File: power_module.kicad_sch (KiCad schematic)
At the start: 46 parts, among them J1 USB_C_PD, Q1 DUAL_N_FET, Q2 DUAL_N_FET, SW1 OFF, U1 BQ7692003, U2 CH224K, U3 BQ24650

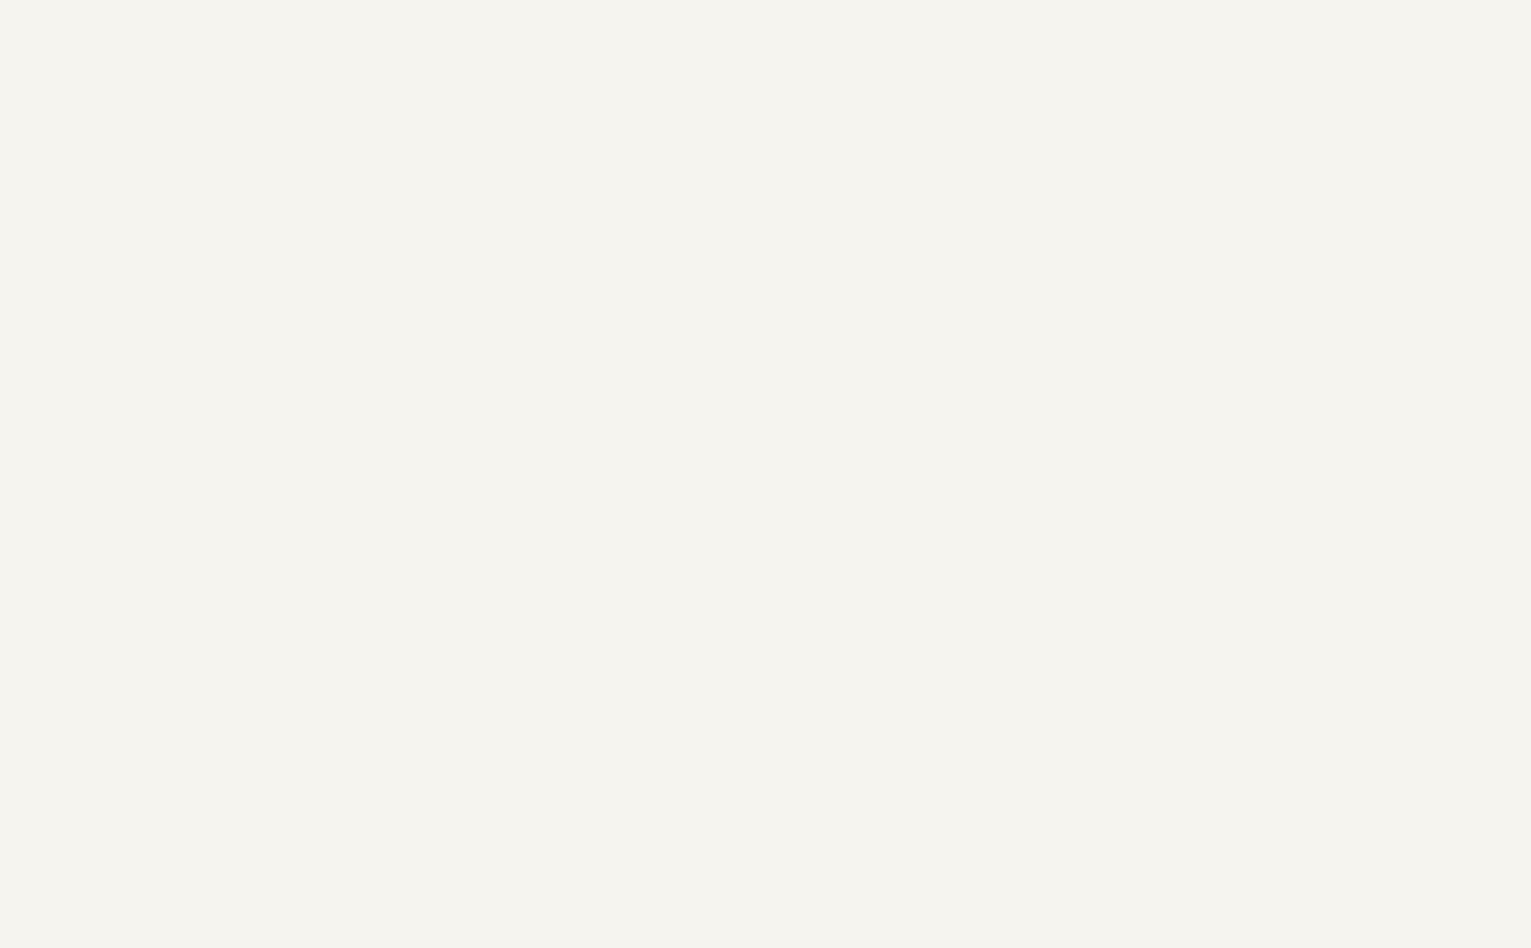
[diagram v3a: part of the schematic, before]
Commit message: schematic: add 4-switch buck-boost output stage (LM5176)
LM5176PWP HTSSOP-28 controller drives 2x dual N-FET pairs (Q3 input,
Q4 output) through inductor L2 (10 µH).  Topology:
  BAT+ → Q3a (HS_IN) → SW1 → L2 → SW2 → Q4b (HS_OUT) → V12_OUT
                ↓                          ↓
         Q3b (LS_IN)→GND          Q4a (LS_OUT)→GND
  + ISNS shunt R20 (5 mΩ) between Q4b drain and V12_OUT load.

Regulation: VFB divider R21=90k / R22=10k → 12 V at FB=1.207 V.
Soft-start C22=10 nF, RT/SYNC R25=22k (~440 kHz), Type II compensation
C20/R26/C21 on COMP, slope cap C31=47 pF.  Mode pin tied to GND for
auto-PFM at light load.

Power: input bulk + HF caps on BAT+ side (C27/C28), output bulk + HF
on V12_OUT (C29/C30), bootstrap caps C23/C24 between BOOT and SW.
VCC self-biased: BIAS tied to VCC, both filtered with C25/C26.

Telemetry: PGOOD-fault LED D2 with 1k current-limit R27 between
BB_VCC and PGOOD pin (open-drain pulls low on fault, lights LED).

Wiring used the new connect_pins(style="auto") path; the autorouter
drew real wires for ~10 pairs (straight / L / U / A* / A*-tee styles
in the result), with labels falling back where geometry didn't allow
a clean wire.  PWR_FLAG #FLG4 on BB_VCC (chip-internal regulator) so
ERC accepts the BB_VCC net as power-driven.  Unused DITH pin marked
no_connect.

ERC: 2 errors remain (SW1 placeholder pins from BMS subcircuit,
intentional).  1 footprint warning still on the charger inductor
(L_Bourns_SRR1280 not in default library) — will pick a generic
SMD inductor footprint at the LCSC-property assignment step.

Layout note: first attempt placed several support passives inside
U4's body bbox (LM5176 is a large ~36×46 mm symbol).  Repositioned
with explicit zones (LEFT for input filter / EN, RIGHT for output
filter / LED, BELOW for control/comp/SS/RT/FB) and ≥5 mm spacing.

Co-Authored-By: Claude Opus 4.7 <noreply@anthropic.com>
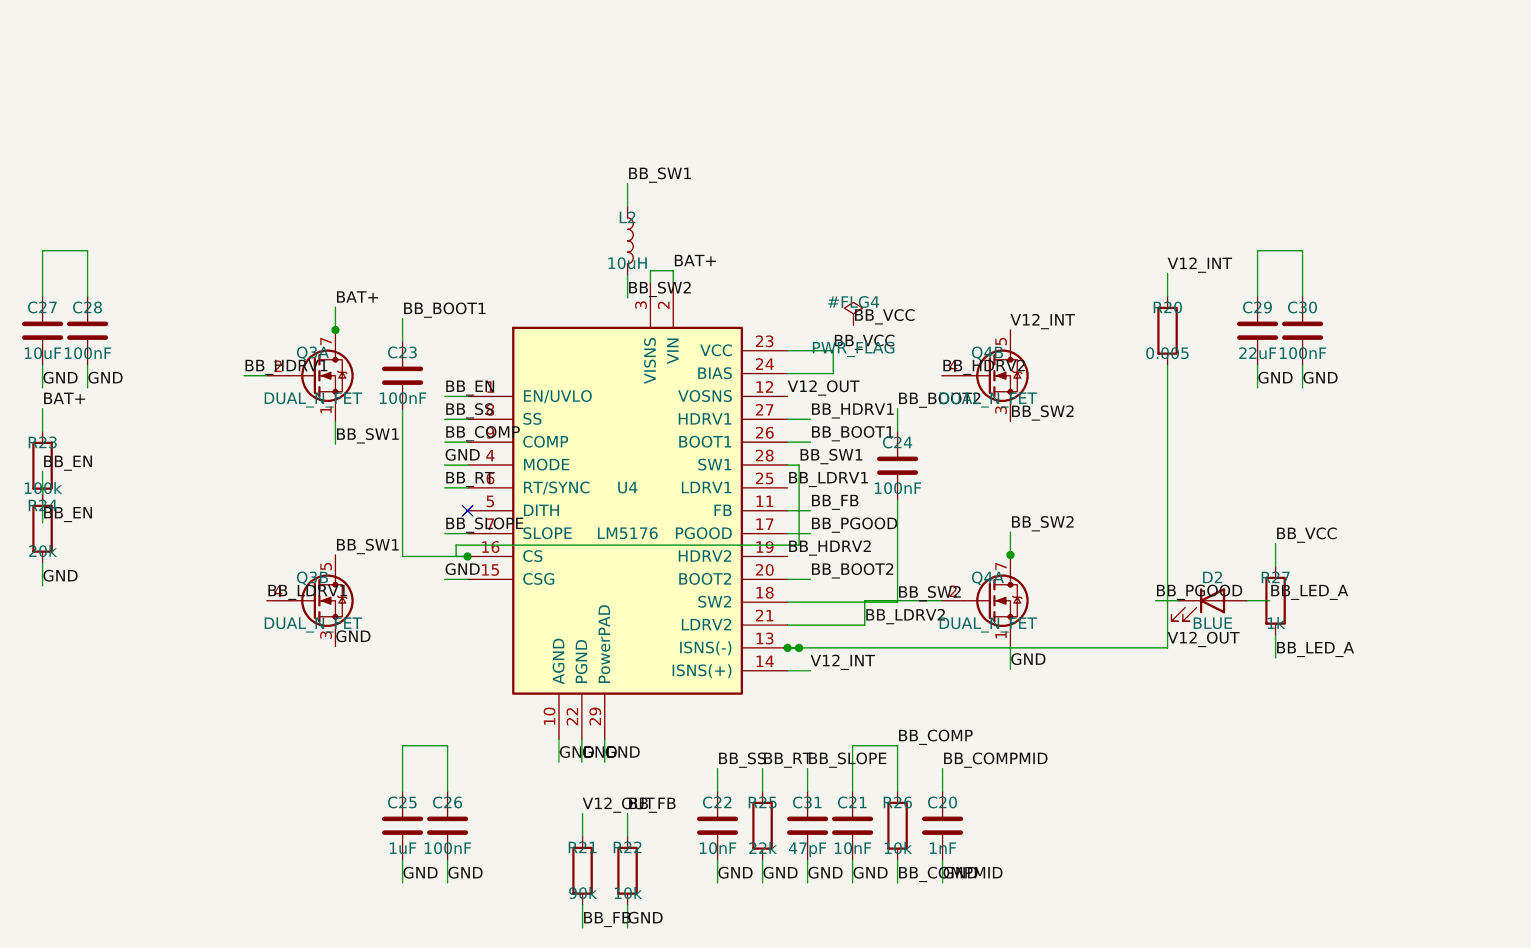
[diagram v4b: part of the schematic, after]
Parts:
- added C20: 1nF, symbol Device:C
- added C21, C22: 10nF, symbol Device:C
- added C23, C24, C26, C28, C30: 100nF, symbol Device:C
- added C25: 1uF, symbol Device:C
- added C27: 10uF, symbol Device:C
- added C29: 22uF, symbol Device:C
- added C31: 47pF, symbol Device:C
- added D2: BLUE, LED_SMD:LED_0805_2012Metric, symbol Device:LED
- added L2: 10uH, Inductor_SMD:L_12x12mm_H8mm, symbol Device:L
- added Q3, Q4: DUAL_N_FET, symbol Transistor_FET:FDS9926A
- added R20: 0.005, Resistor_SMD:R_2512_6332Metric, symbol Device:R
- added R21: 90k, symbol Device:R
- added R22, R26: 10k, symbol Device:R
- added R23: 100k, symbol Device:R
- added R24: 20k, symbol Device:R
- added R25: 22k, symbol Device:R
- added R27: 1k, symbol Device:R
- added U4: LM5176, Package_SO:HTSSOP-28-1EP_4.4x9.7mm_P0.65mm_EP3.4x9.5mm_ThermalVias, symbol Regulator_Switching:LM5176PWP
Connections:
- net BAT+: now also Q3.7 (D1), Q3.8 (D1), R23.1, U4.2 (VIN), U4.3 (VISNS)
- net GND: now also C20.2, C21.2, C22.2, C25.2, C26.2, C27.2, C28.2, C29.2, C30.2, C31.2, Q3.3 (S2), Q4.1 (S1), R22.2, R24.2, R25.2, U4.10 (AGND), U4.15 (CSG), U4.22 (PGND), U4.29 (PowerPAD), U4.4 (MODE)
- new net: C25.1, C26.1
- new net: C29.1, C30.1
- new net: C27.1, C28.1
- new net BB_BOOT1: C23.1, U4.26 (BOOT1)
- new net BB_BOOT2: C24.1, U4.20 (BOOT2)
- new net BB_COMP: C21.1, R26.1, U4.9 (COMP)
- new net BB_COMPMID: C20.1, R26.2
- new net BB_EN: R23.2, R24.1, U4.1 (EN/UVLO)
- new net BB_FB: R21.2, R22.1, U4.11 (FB)
- new net BB_HDRV1: Q3.2 (G1), U4.27 (HDRV1)
- new net BB_HDRV2: Q4.4 (G2), U4.19 (HDRV2)
- new net BB_LDRV1: Q3.4 (G2), U4.25 (LDRV1)
- new net BB_LDRV2: Q4.2 (G1), U4.21 (LDRV2)
- new net BB_LED_A: D2.2 (A), R27.2
- new net BB_PGOOD: D2.1 (K), U4.17 (PGOOD)
- new net BB_RT: R25.1, U4.6 (RT/SYNC)
- new net BB_SLOPE: C31.1, U4.7 (SLOPE)
- new net BB_SS: C22.1, U4.8 (SS)
- new net BB_SW1: C23.2, L2.1, Q3.1 (S1), Q3.5 (D2), Q3.6 (D2), U4.16 (CS), U4.28 (SW1)
- new net BB_SW2: C24.2, L2.2, Q4.3 (S2), Q4.7 (D1), Q4.8 (D1), U4.18 (SW2)
- new net BB_VCC: R27.1, U4.23 (VCC), U4.24 (BIAS)
- new net V12_INT: Q4.5 (D2), Q4.6 (D2), R20.1, U4.14 (ISNS(+))
- new net V12_OUT: R20.2, R21.1, U4.12 (VOSNS), U4.13 (ISNS(-))
- no-connect marks 5 -> 6

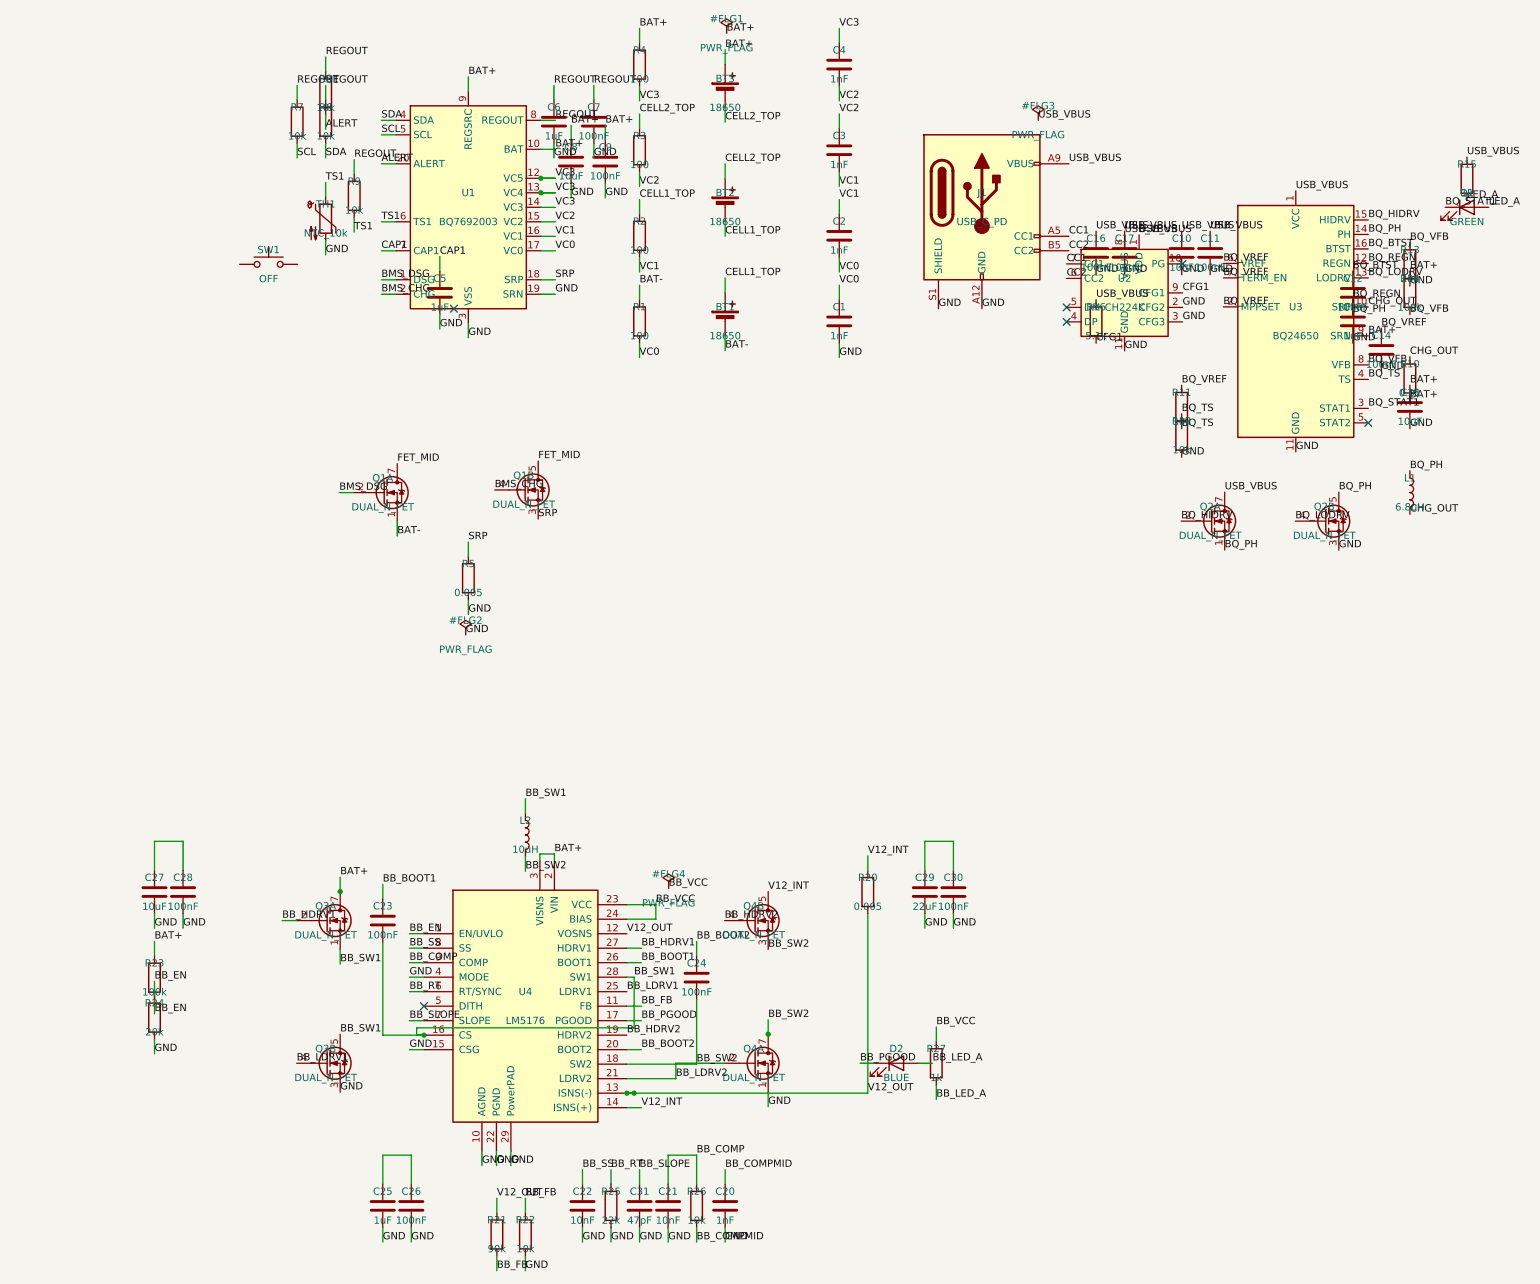
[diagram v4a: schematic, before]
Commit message: schematic: convert flat design into hierarchical sheets
Split the single power_module.kicad_sch into a thin top-level that
holds three sheet blocks (BMS, Charger, Buck-Boost) referencing
sibling files bms.kicad_sch / charger.kicad_sch / buckboost.kicad_sch.

Partition (via /tmp/claude/partition_sheets.py):
  - Components grouped by reference designator into BMS_REFS /
    CHARGER_REFS / BUCKBOOST_REFS buckets (28 / 23 / 28 symbols).
  - Wires kept by BFS from each kept symbol's pin world coords —
    grows the keep-set until no new wires can be reached.
  - Labels / junctions / no_connects kept when their position is
    on a kept-component pin OR a kept-wire endpoint.
  - Each child gets a fresh root UUID (collisions with the parent
    or a sibling would confuse KiCad's per-page annotation).

Cross-sheet wiring:
  - BAT+ and GND labels promoted to global_label in every child.
    KiCad treats global_labels as one net by name without needing
    sheet pins, so the GND / BAT+ rails connect across BMS, Charger,
    and Buck-Boost without explicit hierarchical plumbing.
  - V12_OUT remains a local label on Buck-Boost (will become a
    global / hierarchical label when integration adds the output
    header).

Top-level: started from the empty template, fresh root UUID, three
sheet blocks placed via add_schematic_sheet at (50,50), (130,50),
(210,50) — page numbers 2/3/4 (root is page 1).

Side-effect bug discovered: the autorouter (connect_pins style=auto)
sometimes wires a same-net pin pair into a self-contained chain
that doesn't reach a labeled point, leaving those pins on a
floating sub-net.  Surfaced when partitioning isolated three such
chains in the buck-boost sheet (C27↔C28 BAT+, C25↔C26 BB_VCC,
C29↔C30 V12_OUT).  Fixed by adding labels at the orphaned chain
endpoints; should be tracked as an autorouter improvement (every
component on a net should be connected to the labeled portion of
that net, not just to one other component on it).

ERC: 2 errors at the top 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
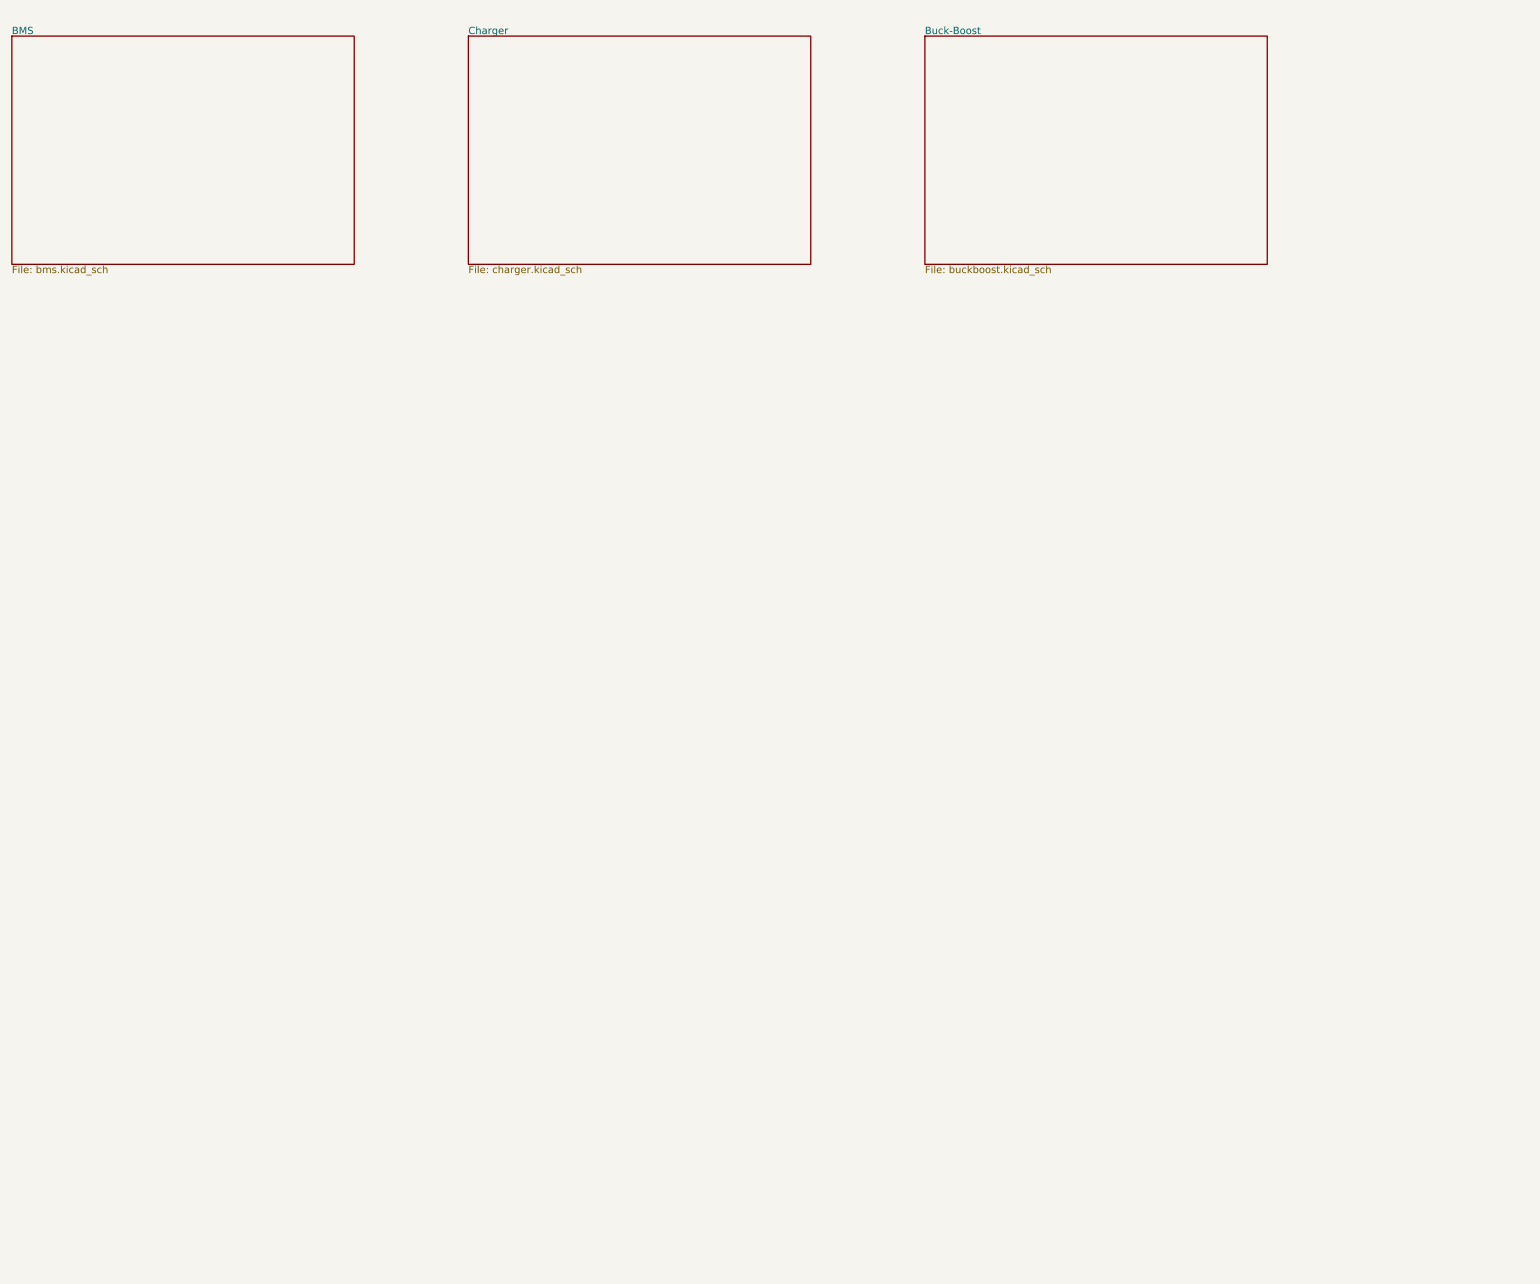
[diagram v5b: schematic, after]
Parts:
- removed BT1, BT2, BT3: 18650, symbol Device:Battery_Cell
- removed C1, C2, C20, C3, C4: 1nF, symbol Device:C
- removed C10, C15, C27, C8: 10uF, symbol Device:C
- removed C11, C12, C14, C16, C17, C23, C24, C26, C28, C30, C7, C9: 100nF, symbol Device:C
- removed C13, C25, C5, C6: 1uF, symbol Device:C
- removed C21, C22: 10nF, symbol Device:C
- removed C29: 22uF, symbol Device:C
- removed C31: 47pF, symbol Device:C
- removed D1: GREEN, LED_SMD:LED_0805_2012Metric, symbol Device:LED
- removed D2: BLUE, LED_SMD:LED_0805_2012Metric, symbol Device:LED
- removed J1: USB_C_PD, Connector_USB:USB_C_Receptacle_HRO_TYPE-C-31-M-12, symbol Connector:USB_C_Receptacle_PowerOnly_24P
- removed L1: 6.8uH, Inductor_SMD:L_Bourns_SRR1280, symbol Device:L
- removed L2: 10uH, Inductor_SMD:L_12x12mm_H8mm, symbol Device:L
- removed Q1, Q2, Q3, Q4: DUAL_N_FET, symbol Transistor_FET:FDS9926A
- removed R1, R2, R3, R4: 100, symbol Device:R
- removed R10: 0.01, Resistor_SMD:R_2512_6332Metric, symbol Device:R
- removed R11, R12, R22, R26, R6, R7, R8, R9: 10k, symbol Device:R
- removed R13, R24: 20k, symbol Device:R
- removed R14, R23: 100k, symbol Device:R
- removed R15, R27: 1k, symbol Device:R
- removed R16: 5.1k, symbol Device:R
- removed R20: 0.005, Resistor_SMD:R_2512_6332Metric, symbol Device:R
- removed R21: 90k, symbol Device:R
- removed R25: 22k, symbol Device:R
- removed R5: 0.005, symbol Device:R
- removed SW1: OFF, symbol Switch:SW_Push
- removed TH1: NTC_10k, symbol Device:Thermistor_NTC
- removed U1: BQ7692003, Package_SO:TSSOP-20_4.4x6.5mm_P0.65mm, symbol Battery_Management:BQ76920PW
- removed U2: CH224K, Package_SO:SSOP-10-1EP_3.9x4.9mm_P1mm_EP2.1x3.3mm, symbol Interface_USB:CH224K
- removed U3: BQ24650, Package_DFN_QFN:Texas_RVA_VQFN-16-1EP_3.5x3.5mm_P0.5mm_EP2.14x2.14mm_ThermalVias, symbol Battery_Management:BQ24650
- removed U4: LM5176, Package_SO:HTSSOP-28-1EP_4.4x9.7mm_P0.65mm_EP3.4x9.5mm_ThermalVias, symbol Regulator_Switching:LM5176PWP
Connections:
- no-connect marks 6 -> 0
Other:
- added sheet BMS (bms.kicad_sch)
- added sheet Buck-Boost (buckboost.kicad_sch)
- added sheet Charger (charger.kicad_sch)
